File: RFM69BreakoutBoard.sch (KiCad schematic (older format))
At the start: 22 parts, among them P1 BB Holes, P10 TST, P11 ANA hole, P2 TST, P3 TST, P4 TST, P5 TST, P6 TST, P7 TST, P8 TST, P9 TST, U1 MCP1703, U2 74LVC245, U3 RFM69HW

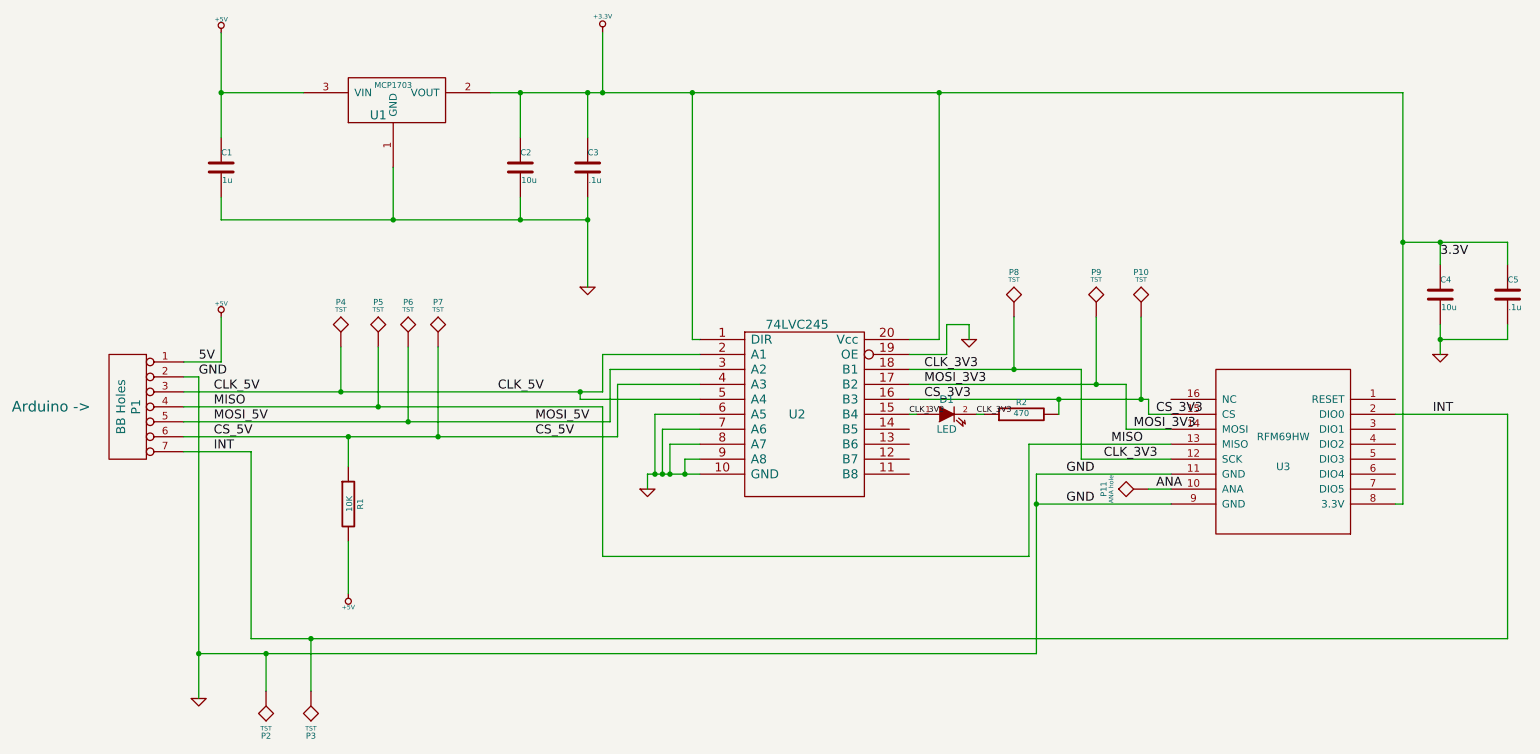
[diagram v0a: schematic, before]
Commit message: removed 74LVC245 level shifter.  Replaced with 74HCT125
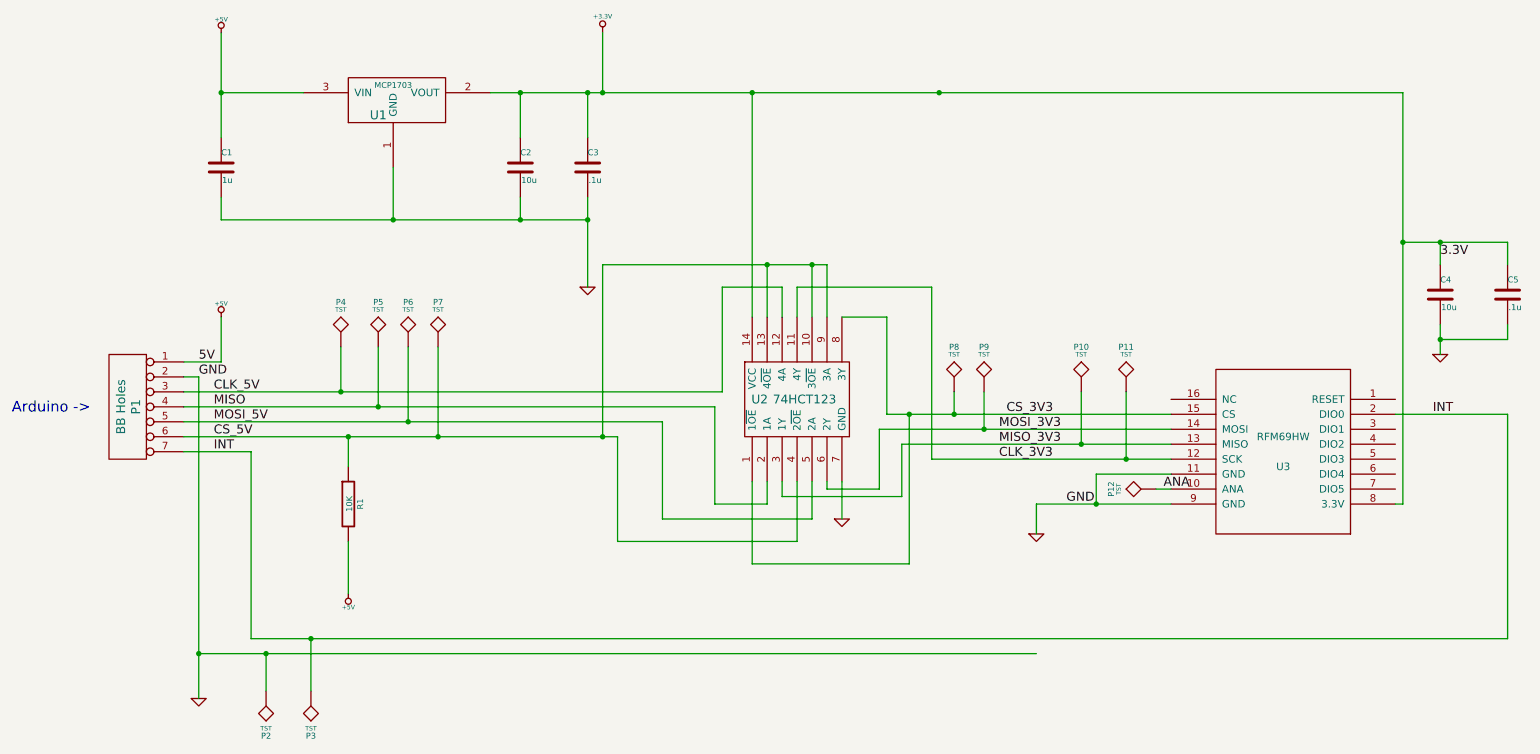
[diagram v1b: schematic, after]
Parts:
- removed D1: LED, ~, symbol LED
- removed R2: 470, ~, symbol R
- removed U2: 74LVC245, ~, symbol 74LVC245
- added P12: TST, ~, symbol TST
- added U2: 74HCT123, symbol 74HCT123
- P11: value ANA hole -> TST
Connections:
- net +3.3V: now also U2.14 (VCC)
- net ANA: now also P12.1; no longer P11.1
- net CLK_3V3: now also P11.1, U2.11 (4Y); no longer P8.1
- net CLK_5V: now also U2.12 (4A)
- net CS_3V3: now also P8.1, U2.1 (1~OE), U2.8 (3Y); no longer P10.1
- net CS_5V: now also U2.10 (3~OE), U2.13 (4~OE), U2.4 (2~OE), U2.9 (3A)
- net GND: now also U2.7 (GND)
- net MISO: now also U2.2 (1A); no longer U3.13 (MISO)
- net MOSI_3V3: now also U2.6 (2Y)
- net MOSI_5V: now also U2.5 (2A)
- new net MISO_3V3: P10.1, U2.3 (1Y), U3.13 (MISO)
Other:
- moved on the sheet: P10, P8, P9

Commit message: notice errors in schematic - updated schematic to fix
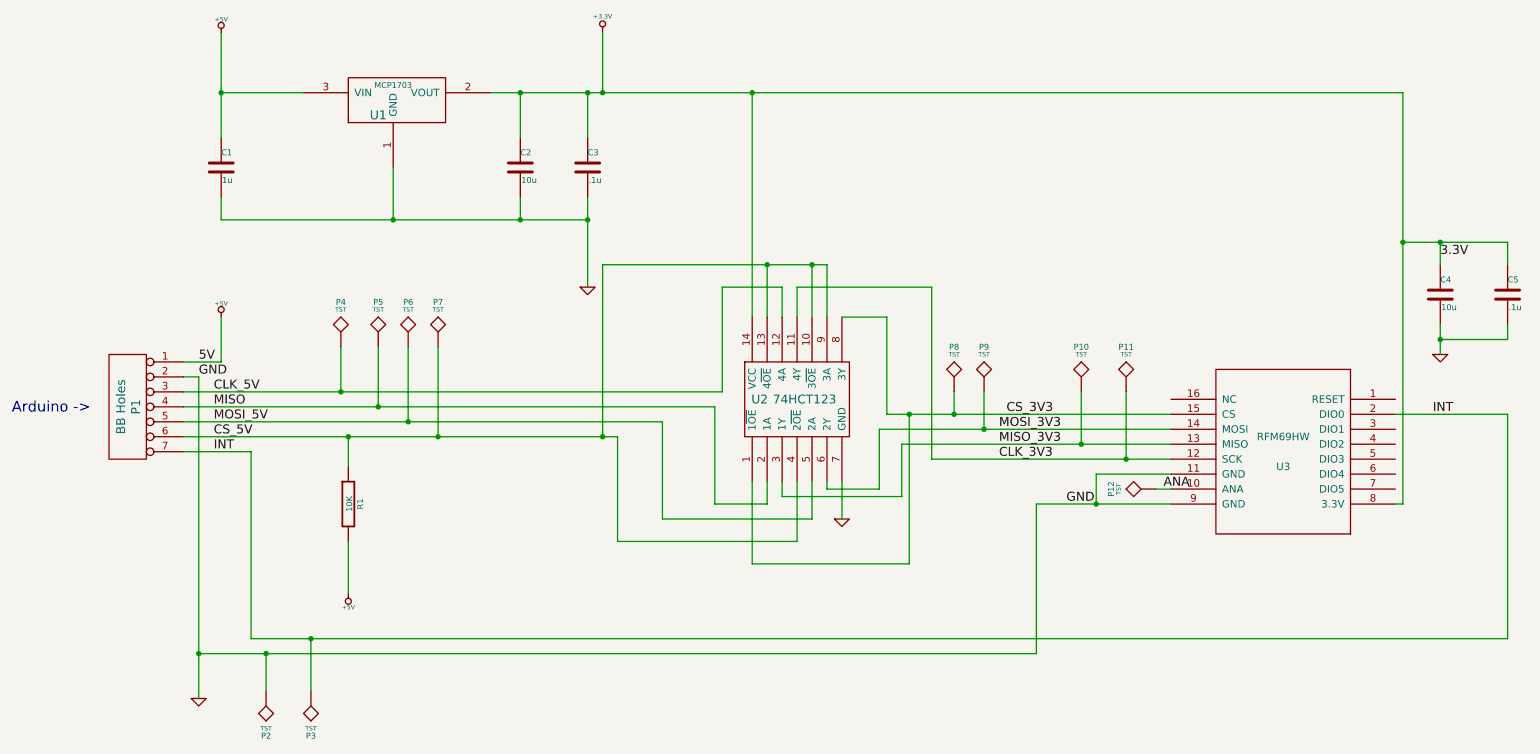
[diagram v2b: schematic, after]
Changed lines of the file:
@@
 Sheet 1 1
 Title ""
-Date "7 mar 2014"
+Date "8 mar 2014"
 Rev ""
 Comp ""
@@
 CLK_3V3
 $Comp
-L GND #PWR09
-U 1 1 5319E5C9
-P 7400 5250
-F 0 "#PWR09" H 7400 5250 30  0001 C CNN
-F 1 "GND" H 7400 5180 30  0001 C CNN
-F 2 "" H 7400 5250 60  0000 C CNN
-F 3 "" H 7400 5250 60  0000 C CNN
-	1    7400 5250
-	1    0    0    -1
-$EndComp
-$Comp
 L TST P11
 U 1 1 5319E822
@@
 	1950 3150 4400 3150
 Connection ~ 4400 3150
-Connection ~ 6750 2300
 Wire Wire Line
 	9850 2300 9850 5050
@@
 	2150 5950 10550 5950
 Wire Wire Line
-	1800 6050 7400 6050
+	7400 6050 1800 6050
 Connection ~ 1800 6050
 Wire Wire Line
@@
 Connection ~ 7800 5050
 Wire Wire Line
-	7400 5050 7400 5250
+	7400 5050 7400 6050
 Wire Wire Line
 	6850 4450 6850 4300
